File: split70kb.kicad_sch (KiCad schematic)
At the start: 2 parts, among them U1 ATMEGA32U4, X1 XTAL_GND

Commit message: finish schematic and pcb layout
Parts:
- added C1, C2: 22p, Capacitor_SMD:C_0805_2012Metric, symbol Device:C_Small
- added C3, C4, C5, C6, C7: 0.1u, Capacitor_SMD:C_0805_2012Metric, symbol Device:C_Small
- added C8: 1u, Capacitor_SMD:C_0805_2012Metric, symbol Device:C_Small
- added D1, D10, D11, D12, D13, D14, D15, D16, D17, D18, D19, D2, D20, D21, D22, D23, D24, D25, D26, D27, D28, D29, D3, D30, D31, D32, D33, D34, D35, D4, D5, D6, D7, D8, D9: D, keyboard_parts.pretty-master:D_SOD123_axial, symbol Device:D
- added J1: USB_C_Receptacle_USB2.0, Connector_USB:USB_C_Receptacle_Molex_105450-0101, symbol Connector:USB_C_Receptacle_USB2.0
- added J2: AudioJack4, Connector_Audio:Jack_3.5mm_PJ320D_Horizontal, symbol Connector_Audio:AudioJack4
- added K1, K10, K11, K12, K13, K14, K15, K16, K17, K18, K19, K2, K20, K21, K22, K23, K24, K25, K26, K27, K28, K29, K3, K30, K31, K32, K33, K34, K35, K4, K5, K6, K7, K8, K9: KEYSW, keyboard_parts.pretty-master:Mx_Alps_100, symbol keyboard_parts:KEYSW
- added R1, R2: 10k, Resistor_SMD:R_0805_2012Metric, symbol Device:R
- added R3, R4: 22, Resistor_SMD:R_0805_2012Metric, symbol Device:R
- added R5, R6: 5.1K, Resistor_SMD:R_0805_2012Metric, symbol Device:R
- added SW1: SW_PUSH, Button_Switch_SMD:SW_SPST_TL3342, symbol keyboard_parts:SW_PUSH
- U1: footprint (none) -> Package_QFP:TQFP-44_10x10mm_P0.8mm
- X1: footprint (none) -> Crystal:Crystal_SMD_SeikoEpson_FA238-4Pin_3.2x2.5mm
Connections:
- net +5V is gone; now on net GND: X1.3
- net at X1.1: now also U1.16 (XTAL1), C1.1
- net at X1.2: now also U1.17 (XTAL2), C2.1
- net at U1.13 (~{RESET}): now also R1.2, SW1.2
- net pd2: now reaches U1.20 (PD2/RXD1)
- net pd2: now also J2.R1
- net GND: now reaches U1.23 (GND)
- net GND: now also U1.35 (GND), U1.43 (GND), U1.5 (UGnd), C1.2, C2.2, C3.2, C4.2, C5.2, C6.2, C7.2, C8.1, J1.A1 (GND), J1.A12 (GND), J1.B1 (GND), J1.B12 (GND), J1.S1 (SHIELD), J2.S, R2.1, R5.1, R6.2, SW1.1
- net VCC: now reaches U1.24 (AVCC)
- net VCC: now also U1.34 (VCC), U1.44 (AVCC), U1.7 (VBus), C3.1, C4.1, C5.1, C6.1, C7.1, J1.A4 (VBUS), J1.A9 (VBUS), J1.B4 (VBUS), J1.B9 (VBUS), J2.R2, R1.1
- net col5: now reaches U1.27 (T0/PD7)
- net col5: now also U1.28 (PB4), U1.29 (PB5), U1.37 (PF6), U1.38 (PF5), U1.39 (PF4), U1.40 (PF1), U1.41 (PF0), D1.1 (K), D10.1 (K), D11.1 (K), D12.1 (K), D13.1 (K), D14.1 (K), D15.1 (K), D16.1 (K), D17.1 (K), D18.1 (K), D19.1 (K), D2.1 (K), D20.1 (K), D21.1 (K), D22.1 (K), D23.1 (K), D24.1 (K), D25.1 (K), D26.1 (K), D27.1 (K), D28.1 (K), D29.1 (K), D3.1 (K), D30.1 (K), D31.1 (K), D32.1 (K), D33.1 (K), D34.1 (K), D35.1 (K), D4.1 (K), D5.1 (K), D6.1 (K), D7.1 (K), D8.1 (K), D9.1 (K), K21.1, K22.1, K23.1, K24.1, K25.1, K26.1, K27.1, K28.1, K29.1, K30.1, K31.1, K32.1, K33.1, K34.1, K35.1
- net at U1.3 (D-): now also R4.2
- net col4: now reaches U1.30 (PB6)
- net col4: now also K16.1, K17.1, K18.1, K19.1, K20.1
- net col3: now reaches U1.31 (PC6)
- net col3: now also K11.1, K12.1, K13.1, K14.1, K15.1
- net col2: now reaches U1.32 (PC7)
- net col2: now also K10.1, K6.1, K7.1, K8.1, K9.1
- net at U1.33 (~{HWB/PE2}): now also R2.2
- net col1: now reaches U1.36 (PF7)
- net col1: now also K1.1, K2.1, K3.1, K4.1, K5.1
- net at U1.4 (D+): now also R3.1
- net at U1.6 (UCap): now also C8.2
- new net: D5.2 (A), K5.2
- new net: D19.2 (A), K19.2
- new net: D7.2 (A), K7.2
- new net: D17.2 (A), K17.2
- new net: D25.2 (A), K25.2
- new net: D22.2 (A), K22.2
- new net: D35.2 (A), K35.2
- new net: D23.2 (A), K23.2
- new net: D8.2 (A), K8.2
- new net: D21.2 (A), K21.2
- new net: D3.2 (A), K3.2
- new net: D32.2 (A), K32.2
- new net: D29.2 (A), K29.2
- new net: D20.2 (A), K20.2
- new net: D34.2 (A), K34.2
- new net: D16.2 (A), K16.2
- new net: D1.2 (A), K1.2
- new net: D9.2 (A), K9.2
- new net: D27.2 (A), K27.2
- new net: D18.2 (A), K18.2
- new net: D14.2 (A), K14.2
- new net: D10.2 (A), K10.2
- new net: D11.2 (A), K11.2
- new net: D28.2 (A), K28.2
- new net: J1.B5 (CC2), R6.1
- new net: D26.2 (A), K26.2
- new net: D6.2 (A), K6.2
- new net: D33.2 (A), K33.2
- new net: J1.A6 (D+), J1.B6 (D+), R3.2
- new net: D12.2 (A), K12.2
- new net: J1.A5 (CC1), R5.2
- new net: J1.A7 (D-), J1.B7 (D-), R4.1
- new net: D2.2 (A), K2.2
- new net: D31.2 (A), K31.2
- new net: D13.2 (A), K13.2
- new net: D30.2 (A), K30.2
- new net: D15.2 (A), K15.2
- new net: D4.2 (A), K4.2
- new net: D24.2 (A), K24.2
- no-connect marks 0 -> 18
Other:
- moved on the sheet: U1, X1

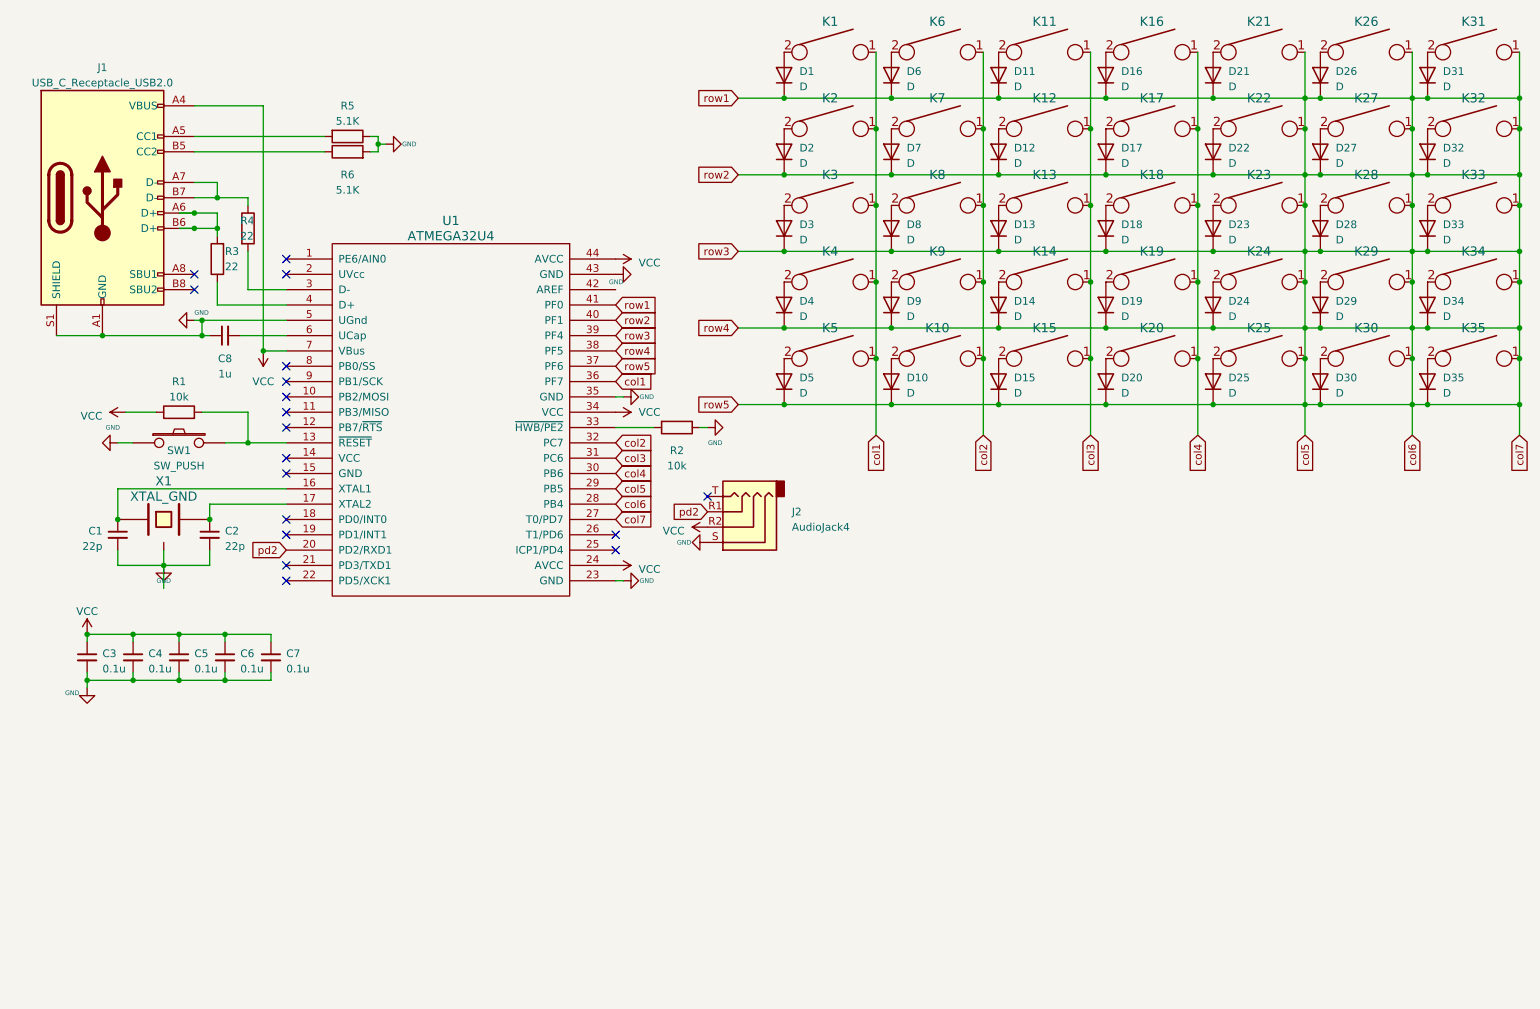
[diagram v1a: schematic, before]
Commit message: update for right side too in one board
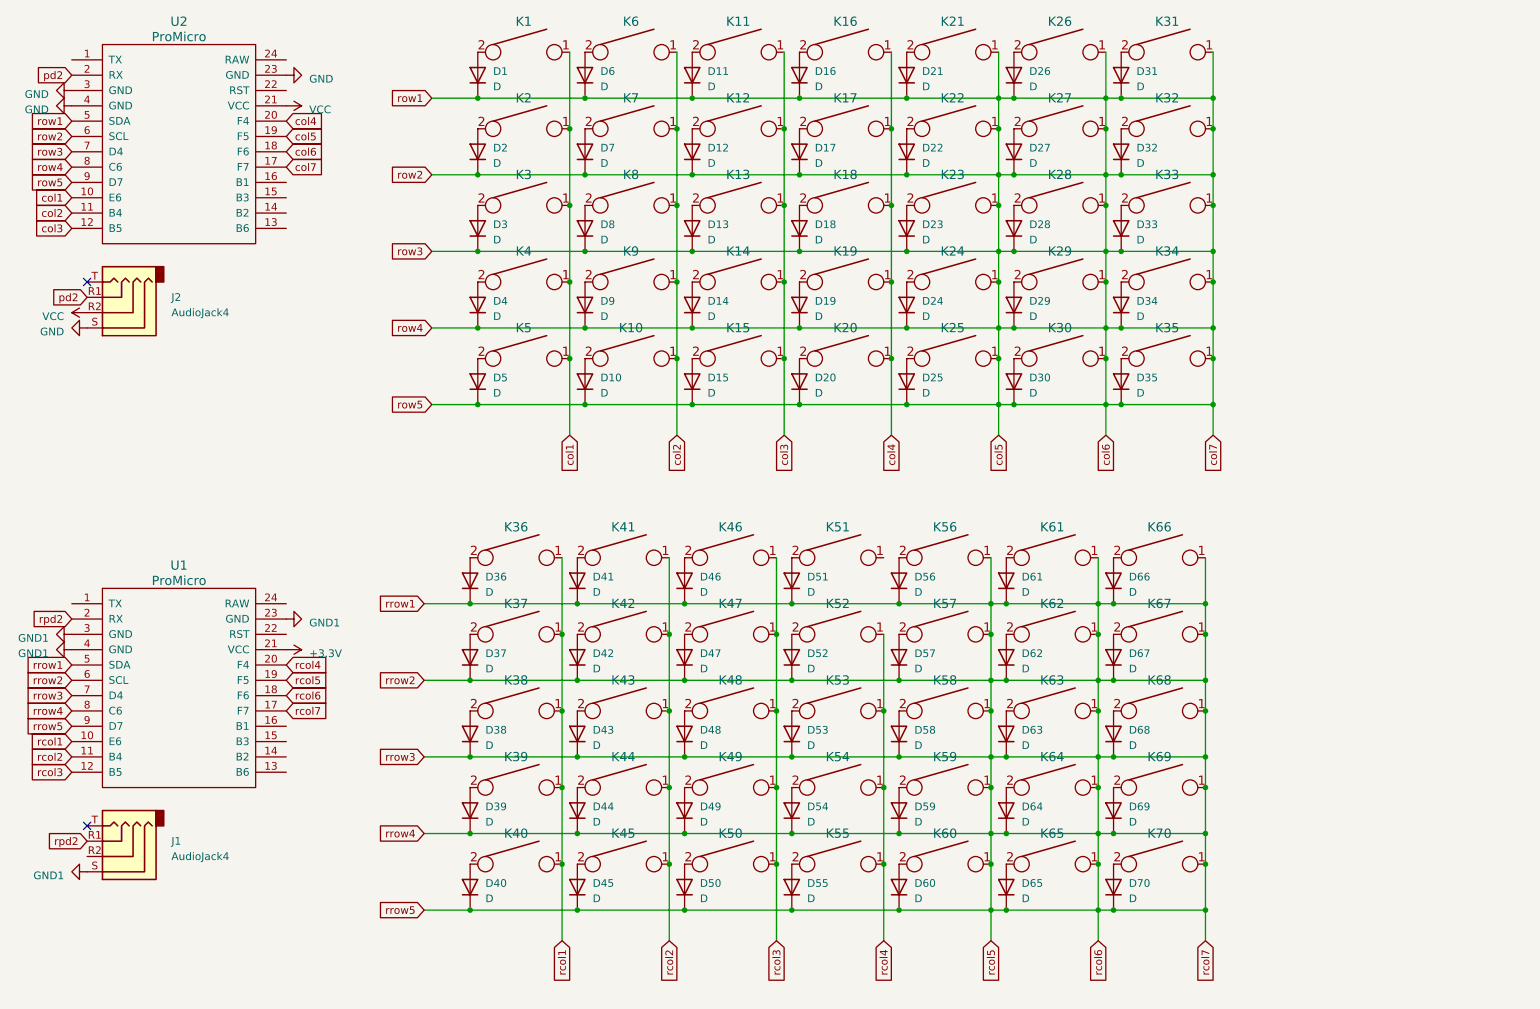
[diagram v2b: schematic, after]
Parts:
- removed C1, C2: 22p, Capacitor_SMD:C_0805_2012Metric, symbol Device:C_Small
- removed C3, C4, C5, C6, C7: 0.1u, Capacitor_SMD:C_0805_2012Metric, symbol Device:C_Small
- removed C8: 1u, Capacitor_SMD:C_0805_2012Metric, symbol Device:C_Small
- removed J1: USB_C_Receptacle_USB2.0, Connector_USB:USB_C_Receptacle_Molex_105450-0101, symbol Connector:USB_C_Receptacle_USB2.0
- removed R1, R2: 10k, Resistor_SMD:R_0805_2012Metric, symbol Device:R
- removed R3, R4: 22, Resistor_SMD:R_0805_2012Metric, symbol Device:R
- removed R5, R6: 5.1K, Resistor_SMD:R_0805_2012Metric, symbol Device:R
- removed SW1: SW_PUSH, Button_Switch_SMD:SW_SPST_TL3342, symbol keyboard_parts:SW_PUSH
- removed U1: ATMEGA32U4, Package_QFP:TQFP-44_10x10mm_P0.8mm, symbol keyboard_parts:ATMEGA32U4
- removed X1: XTAL_GND, Crystal:Crystal_SMD_SeikoEpson_FA238-4Pin_3.2x2.5mm, symbol keyboard_parts:XTAL_GND
- added D36, D37, D38, D39, D40, D41, D42, D43, D44, D45, D46, D47, D48, D49, D50, D51, D52, D53, D54, D55, D56, D57, D58, D59, D60, D61, D62, D63, D64, D65, D66, D67, D68, D69, D70: D, keyboard_parts.pretty-master:D_SOD123_axial, symbol Device:D
- added J1: AudioJack4, Connector_Audio:Jack_3.5mm_PJ320D_Horizontal, symbol Connector_Audio:AudioJack4
- added K36, K37, K38, K39, K40, K41, K42, K43, K44, K45, K46, K47, K48, K49, K50, K51, K52, K53, K54, K55, K56, K57, K58, K59, K60, K61, K62, K63, K64, K65, K66, K67, K68, K69, K70: KEYSW, keyboard_parts.pretty-master:Mx_Alps_100, symbol keyboard_parts:KEYSW
- added U1, U2: ProMicro, keyboard_parts.pretty-master:Pro_Micro, symbol promicro:ProMicro
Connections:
- net GND: now also U2.23 (GND), U2.3 (GND), U2.4 (GND)
- net VCC: now also U2.21 (VCC)
- net col1: now also U2.10 (E6)
- net col2: now also U2.11 (B4)
- net col3: now also U2.12 (B5)
- net col4: now also U2.20 (F4)
- net col5: now also U2.17 (F7), U2.18 (F6), U2.19 (F5), U2.5 (SDA), U2.6 (SCL), U2.7 (D4), U2.8 (C6), U2.9 (D7)
- net pd2: now also U2.2 (RX)
- new net: D61.2 (A), K61.2
- new net: D68.2 (A), K68.2
- new net: D55.2 (A), K55.2
- new net: D36.2 (A), K36.2
- new net: D59.2 (A), K59.2
- new net: D57.2 (A), K57.2
- new net: D69.2 (A), K69.2
- new net: D67.2 (A), K67.2
- new net: D63.2 (A), K63.2
- new net: D44.2 (A), K44.2
- new net: D42.2 (A), K42.2
- new net: D38.2 (A), K38.2
- new net: D46.2 (A), K46.2
- new net: D48.2 (A), K48.2
- new net: D49.2 (A), K49.2
- new net: D65.2 (A), K65.2
- new net: D66.2 (A), K66.2
- new net: D58.2 (A), K58.2
- new net: D37.2 (A), K37.2
- new net: D40.2 (A), K40.2
- new net: D62.2 (A), K62.2
- new net: D53.2 (A), K53.2
- new net: D45.2 (A), K45.2
- new net: D60.2 (A), K60.2
- new net: D70.2 (A), K70.2
- new net: D51.2 (A), K51.2
- new net: D41.2 (A), K41.2
- new net: D56.2 (A), K56.2
- new net: D43.2 (A), K43.2
- new net: D47.2 (A), K47.2
- new net: D52.2 (A), K52.2
- new net: D64.2 (A), K64.2
- new net: D39.2 (A), K39.2
- new net: D50.2 (A), K50.2
- new net: D54.2 (A), K54.2
- new net +3.3V: U1.21 (VCC)
- new net GND1: J1.S, U1.23 (GND), U1.3 (GND), U1.4 (GND)
- new net rcol1: K36.1, K37.1, K38.1, K39.1, K40.1, U1.10 (E6)
- new net rcol2: K41.1, K42.1, K43.1, K44.1, K45.1, U1.11 (B4)
- new net rcol3: K46.1, K47.1, K48.1, K49.1, K50.1, U1.12 (B5)
- new net rcol4: K52.1, K53.1, K54.1, K55.1, U1.20 (F4)
- new net rcol5: D36.1 (K), D37.1 (K), D38.1 (K), D39.1 (K), D40.1 (K), D41.1 (K), D42.1 (K), D43.1 (K), D44.1 (K), D45.1 (K), D46.1 (K), D47.1 (K), D48.1 (K), D49.1 (K), D50.1 (K), D51.1 (K), D52.1 (K), D53.1 (K), D54.1 (K), D55.1 (K), D56.1 (K), D57.1 (K), D58.1 (K), D59.1 (K), D60.1 (K), D61.1 (K), D62.1 (K), D63.1 (K), D64.1 (K), D65.1 (K), D66.1 (K), D67.1 (K), D68.1 (K), D69.1 (K), D70.1 (K), K56.1, K57.1, K58.1, K59.1, K60.1, K61.1, K62.1, K63.1, K64.1, K65.1, K66.1, K67.1, K68.1, K69.1, K70.1, U1.17 (F7), U1.18 (F6), U1.19 (F5), U1.5 (SDA), U1.6 (SCL), U1.7 (D4), U1.8 (C6), U1.9 (D7)
- new net rpd2: J1.R1, U1.2 (RX)
- no-connect marks 18 -> 2
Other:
- moved on the sheet: D1, D10, D11, D12, D13, D14, D15, D16, D17, D18, D19, D2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
